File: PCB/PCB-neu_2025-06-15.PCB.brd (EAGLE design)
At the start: 60 x 60 mm, 16 parts

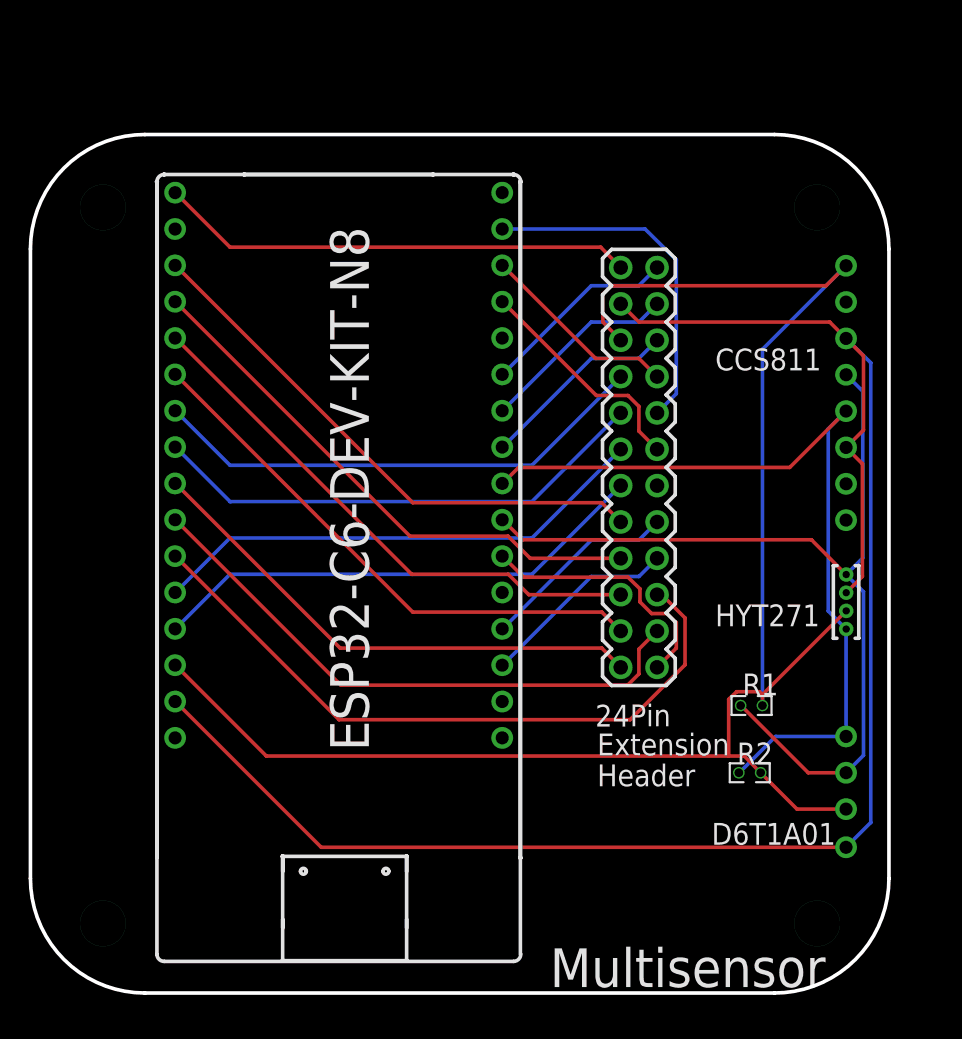
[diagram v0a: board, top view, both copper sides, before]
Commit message: PCB-Update (->Anschlüsse auf Bottom-Layer)
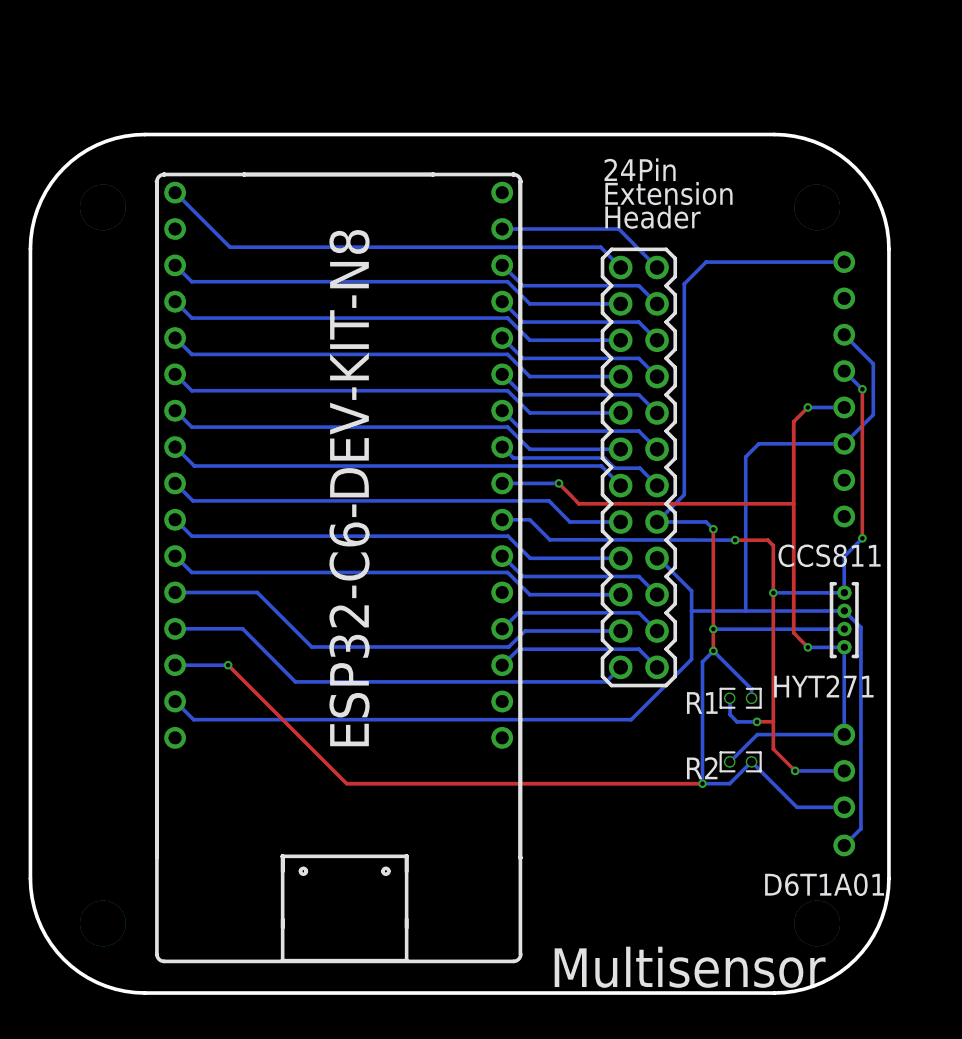
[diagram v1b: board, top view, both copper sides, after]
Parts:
- removed DHDYFYKT: (no value), PCB-verbesserung_2025-06-02 (2):DHDYFYKT_1PRIMARY
- removed ESP32C6: ESP32-C6-DEV-KIT, PCB-verbesserung_2025-06-02 (2):ESP32-C6-DEV-KIT-N8_1PRIMARY
- added ESP32-C6-DEVKITC-1: ESP32-C6-DEV-KIT, PCB-neu_2025-06-15:ESP32-C6-DEV-KIT-N8_1PRIMARY
- added WAAYAVHK: (no value), PCB-neu_2025-06-15:WAAYAVHK_1PRIMARY
- 24: device PCB-verbesserung_2025-06-02 (2):PIN-HEADER-210S-2X12P_WK_1PRIMARY -> PCB-neu_2025-06-15:PIN-HEADER-210S-2X12P_WK_1PRIMARY
- CCS811: device PCB-verbesserung_2025-06-02 (2):CCS811_JOY-IT_1PRIMARY -> PCB-neu_2025-06-15:CCS811_JOY-IT_1PRIMARY
- D6T1A01: device PCB-verbesserung_2025-06-02 (2):D6T1A01_1PRIMARY -> PCB-neu_2025-06-15:D6T1A01_1PRIMARY
- DUMMY1, DUMMY2, DUMMY3, DUMMY4: device PCB-verbesserung_2025-06-02 (2):P:EX40Y40D201 -> PCB-neu_2025-06-15:P:EX40Y40D201
- DUMMY5, DUMMY6, DUMMY7, DUMMY8: device PCB-verbesserung_2025-06-02 (2):P:EX126Y126D1261 -> PCB-neu_2025-06-15:P:EX126Y126D1261
- HYT271: device PCB-verbesserung_2025-06-02 (2):HYT271_1PRIMARY -> PCB-neu_2025-06-15:HYT271_1PRIMARY
- R1, R2: device PCB-verbesserung_2025-06-02 (2):R0603_1PRIMARY -> PCB-neu_2025-06-15:R0603_1PRIMARY
- moved DUMMY3 1.28 mm to (95.1, 63.7)
- moved DUMMY1 1.28 mm to (95.1, 66.2)
- moved DUMMY2 1.28 mm to (95.1, 64.9)
- moved DUMMY4 1.28 mm to (95.1, 62.4)
- moved HYT271 1.28 mm to (95.1, 66.2)
- moved R2 0.99 mm to (87.9, 54.4)
- moved R1 0.92 mm to (87.9, 58.8)
- moved CCS811 0.28 mm to (95.1, 89.3)
- moved D6T1A01 0.18 mm to (95.1, 56.3)
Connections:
- removed net GPIO14: 24.7
- new net GPIO23: 24.4, ESP32-C6-DEVKITC-1.28
- net 3V3: now also ESP32-C6-DEVKITC-1.1; no longer ESP32C6.1
- net 5V0: now also 24.8, ESP32-C6-DEVKITC-1.14; no longer 24.15, ESP32C6.14
- net GND: now also 24.9, ESP32-C6-DEVKITC-1.15; no longer 24.14, ESP32C6.15
- net GPIO0: now also 24.18, ESP32-C6-DEVKITC-1.7; no longer 24.16, ESP32C6.7
- net GPIO1: now also 24.19, ESP32-C6-DEVKITC-1.8; no longer 24.17, ESP32C6.8
- net GPIO10: now also 24.21, ESP32-C6-DEVKITC-1.10; no longer 24.11, ESP32C6.10
- net GPIO11: now also 24.22, ESP32-C6-DEVKITC-1.11; no longer 24.10, ESP32C6.11
- net GPIO12: now also 24.12, ESP32-C6-DEVKITC-1.19; no longer 24.9, ESP32C6.19
- net GPIO13: now also 24.11, ESP32-C6-DEVKITC-1.20; no longer 24.8, ESP32C6.20
- net GPIO15: now also 24.3, ESP32-C6-DEVKITC-1.29; no longer 24.6, ESP32C6.29
- net GPIO16: now also 24.1, ESP32-C6-DEVKITC-1.31; no longer 24.5, ESP32C6.31
- net GPIO17: now also 24.2, ESP32-C6-DEVKITC-1.30; no longer 24.4, ESP32C6.30
- net GPIO2: now also 24.23, ESP32-C6-DEVKITC-1.12; no longer 24.18, ESP32C6.12
- net GPIO20: now also 24.7, ESP32-C6-DEVKITC-1.25; no longer 24.3, ESP32C6.25
- net GPIO21: now also 24.6, ESP32-C6-DEVKITC-1.26; no longer 24.2, ESP32C6.26
- net GPIO22: now also 24.5, ESP32-C6-DEVKITC-1.27; no longer 24.1, ESP32C6.27
- net GPIO3: now also 24.24, ESP32-C6-DEVKITC-1.13; no longer 24.19, ESP32C6.13
- net GPIO4: now also 24.14, ESP32-C6-DEVKITC-1.3; no longer 24.20, ESP32C6.3
- net GPIO5: now also 24.15, ESP32-C6-DEVKITC-1.4; no longer 24.21, ESP32C6.4
- net GPIO6: now also 24.16, ESP32-C6-DEVKITC-1.5; no longer 24.22, ESP32C6.5
- net GPIO7: now also 24.17, ESP32-C6-DEVKITC-1.6; no longer 24.23, ESP32C6.6
- net GPIO8: now also 24.20, ESP32-C6-DEVKITC-1.9; no longer 24.24, ESP32C6.9
- net GPIO9: now also 24.10, ESP32-C6-DEVKITC-1.22; no longer 24.12, ESP32C6.22
- net SCL: now also ESP32-C6-DEVKITC-1.24; no longer ESP32C6.24
- net SDA: now also ESP32-C6-DEVKITC-1.23; no longer ESP32C6.23
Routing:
- net GND: track 124.6 -> 101.8 mm
- net GPIO11: track 47.8 -> 32.2 mm
- net GPIO16: track 24.3 -> 11.9 mm
- net GPIO23: track 0.00 -> 11.9 mm
- net GPIO10: track 41.0 -> 32.2 mm
- net GPIO9: track 18.3 -> 11.9 mm
- net GPIO4: track 38.6 -> 32.2 mm
- net GPIO7: track 38.6 -> 32.2 mm
- net GPIO6: track 38.5 -> 32.2 mm
- net GPIO5: track 38.5 -> 32.2 mm
- net 5V0: track 121.4 -> 117.1 mm, vias 0 -> 5
- net GPIO8: track 36.4 -> 32.2 mm
- net GPIO15: track 16.1 -> 11.9 mm
- net GPIO0: track 35.3 -> 32.2 mm
- net GPIO1: track 35.3 -> 32.2 mm
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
